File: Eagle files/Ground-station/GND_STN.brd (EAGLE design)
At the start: 57.7 x 37.2 mm, 38 parts, among them IC1 BMP280, J2 XT60-M, Q3 SI7625DN-T1-GE3, U1 AMS1117-5.0, U2 AMS1117-3.3, U4 SOIC127P790X216-8NW25Q128JVJSQ, X1 USB Type C

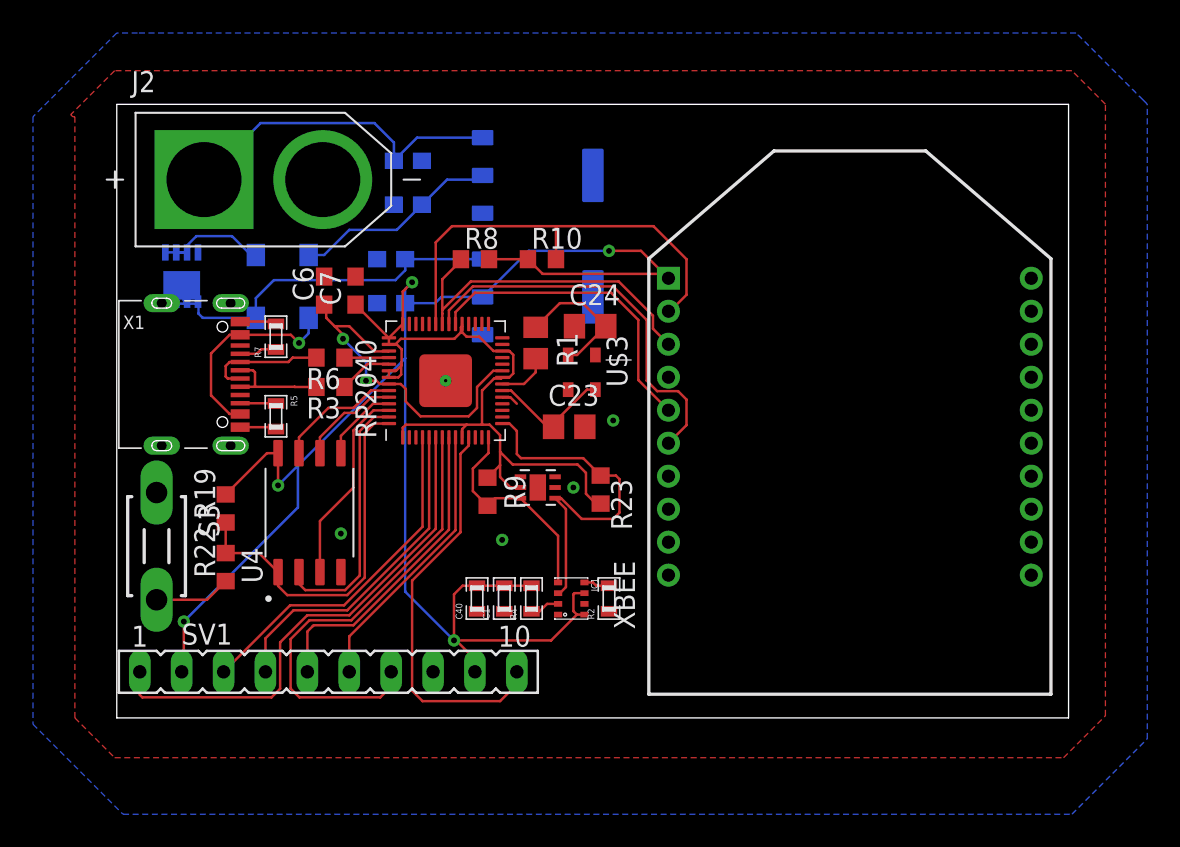
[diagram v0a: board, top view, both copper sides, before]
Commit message: Updated the traces
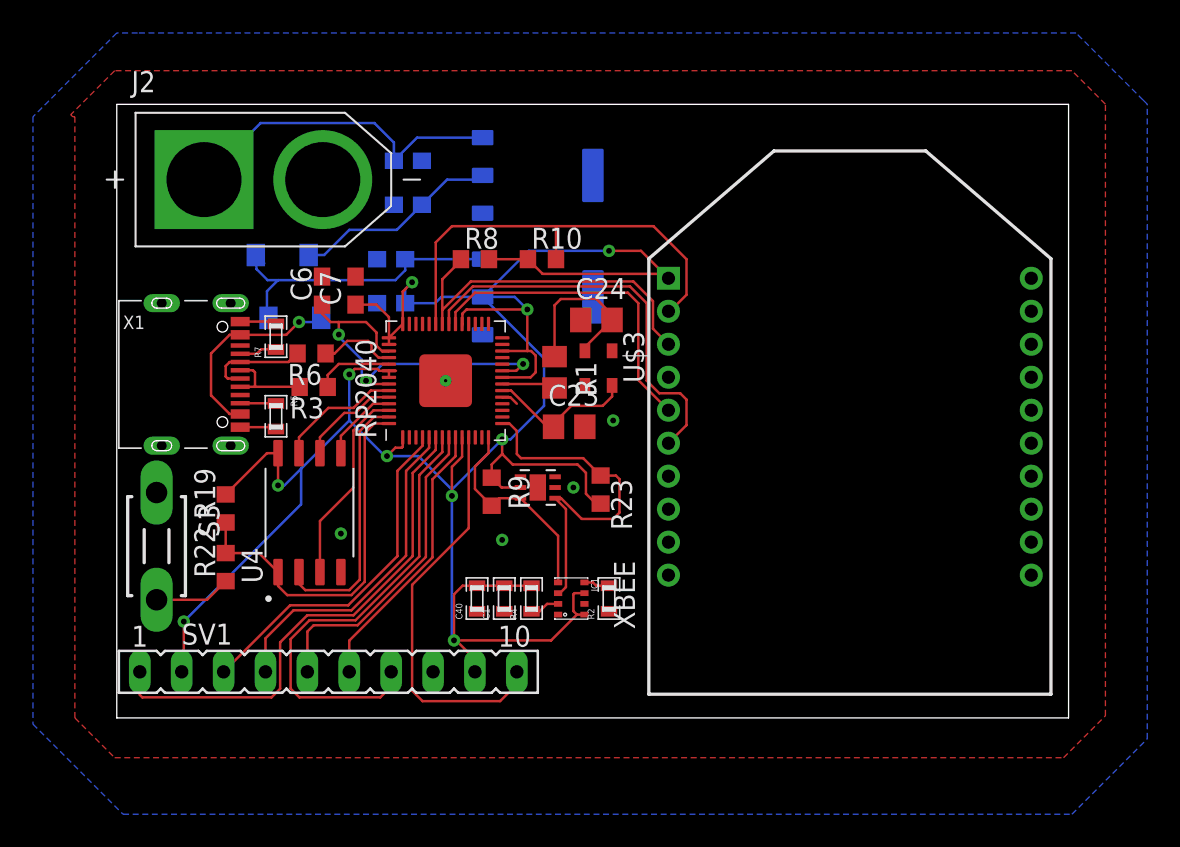
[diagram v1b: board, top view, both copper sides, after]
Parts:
- removed Q3: SI7625DN-T1-GE3, SI7625DN-T1-GE3:SIS862DNT1GE3
- moved R1 2.11 mm to (26.5, 45.5)
- moved R6 1.17 mm to (11.8, 46.6)
- moved U$3 1.05 mm to (29.2, 45.7)
- moved R3 1.02 mm to (11.9, 44.6)
- moved D3 0.76 mm to (10.8, 48.8)
- moved C24 0.54 mm to (29.1, 48.6)
- moved R9 0.25 mm to (22.7, 38.2)
- moved C6 0.13 mm to (12.4, 50.4)
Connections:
- removed net N$1: D4.1, Q3.1, Q3.2, Q3.3
- removed net Q1-G: Q3.4
- net 5V: now also D4.1; no longer Q3.10, Q3.11, Q3.5, Q3.6, Q3.7, Q3.8, Q3.9
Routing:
- net 3V3: track 152.3 -> 159.8 mm, vias 5 -> 10
- net N$1: track 7.28 -> 0.00 mm
- net 5V: track 24.6 -> 19.3 mm
- net N$5: track 2.70 -> 5.16 mm
- net 1V1: track 21.1 -> 23.1 mm, vias 2 -> 3
- net N$6: track 8.44 -> 10.0 mm
- net XIN: track 7.61 -> 9.13 mm
- net N$4: track 3.28 -> 4.72 mm
- net D-: track 7.27 -> 6.24 mm
- net D+: track 6.45 -> 5.44 mm
- net TEL_RST: track 19.2 -> 19.8 mm
- net RSSI: track 23.9 -> 24.5 mm
- net TEL_RX: track 20.9 -> 21.4 mm
